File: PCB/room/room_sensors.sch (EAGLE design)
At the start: 37 parts, among them U1 BH1750FVI-TR, U2 BME280, U3 CCS811B-JOPD500, U4 SN65HVD11DR, U5 SN65HVD11DR, U6 SN65HVD11DR, U7 SN65HVD11DR, U8 MAX14830ETMT

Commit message: first version of schematic ready
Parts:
- removed U$12: NCP551SN18T1G, NCP551SN_snapEDA:NCP551SN18T1G
- removed U$14: NCP551SN25T1G, NCP551SN_snapEDA:NCP551SN25T1G
- added C13, C15, C16, C17, C27, C28, C29: 100nF 50V, rcl:C-EUC0805
- added C14: 1uF 16V, rcl:C-EUC0805
- added C18, C19, C20, C21, C22, C25, C30, C31: 4u7 16V, rcl:C-EUC0805
- added C23, C24: 1u 16V, rcl:C-EUC0805
- added C26: 220p, rcl:C-EUC0805
- added D1, D2, D3, D4: CDSOT23-0502B, CDSOT23-SM712_snapEDA:CDSOT23-SM712
- added R10, R11, R12, R13, R30, R8, R9: 4k7, rcl:R-EU_R1206
- added R14: 0R, rcl:R-EU_R1206
- added R15: 47k, rcl:R-EU_R1206
- added R16: 680R, rcl:R-EU_R1206
- added R17, R18, R20, R21, R23, R24, R26, R27, R29: 1k, rcl:R-EU_R1206
- added R19, R22, R25, R28: 120R, rcl:R-EU_R1206
- added R5: 33k, rcl:R-EU_R1206
- added R6, R7: 100k, rcl:R-EU_R1206
- added U$17, U$18: RT9043GB, NCP551SN_snapEDA:RT9043GB
- added Y1: X1G004171001800 12MHz, X1G0041710033_snapEDA:X1G0041710033
- C10, C9: value 100nF 50V -> 2u2 16V
- C2, C3, C4, C5, C6, C7, C8: device rcl:C-EUC1206 -> rcl:C-EUC0805
- R4: value 100R -> 4k7
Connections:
- removed net +1V8: C11.1, C8.1, U$12.OUT, U$3.DVDD
- removed net +2V5: C12.1, C7.1, U$14.OUT, U$3.AVDD
- new net +1V2: C11.1, C7.1, U$17.FB, U$17.OUT, U$3.DVDD
- new net +2V8: C12.1, C8.1, R6.2, U$18.OUT, U$3.AVDD
- new net AS312_OUT: U$7.REL, U8.*CTS0
- new net CLK_12M: U$3.XVCLK, U$4.MCLK, U8.XIN, Y1.OUT
- new net ESP32_EN1: R5.1, R7.2, U$18.FB
- new net MAX_IO0: U$8.1B, U8.GPIO0
- new net MAX_IO1: U$8.2B, U8.GPIO1
- new net MAX_IO10: U8.GPIO10
- new net MAX_IO11: U8.GPIO11
- new net MAX_IO12: U8.GPIO12
- new net MAX_IO13: U8.GPIO13
- new net MAX_IO14: U8.GPIO14
- new net MAX_IO15: U8.GPIO15
- new net MAX_IO2: U$8.3B, U8.GPIO2
- new net MAX_IO3: U$8.4B, U8.GPIO3
- new net MAX_IO4: U$8.5B, U8.GPIO4
- new net MAX_IO5: U$8.6B, U8.GPIO5
- new net MAX_IO6: U$8.7B, U8.GPIO6
- new net MAX_IO7: U$8.8B, U8.GPIO7
- new net MAX_IO8: U8.GPIO8
- new net MAX_IO9: U8.GPIO9
- new net N$10: U6.D, U8.TX3
- new net N$11: U6.R, U8.RX3
- new net N$12: U4.DE, U4.~RE, U8.*RTS0
- new net N$13: U5.DE, U5.~RE, U8.*RTS1
- new net N$14: C13.1, R12.2, U8.*RST
- new net N$15: U7.DE, U7.~RE, U8.*RTS2
- new net N$16: U6.DE, U6.~RE, U8.*RTS3
- new net N$17: C14.1, U8.V18
- new net N$18: C22.2, U$4.VMID
- new net N$19: U$4.SPKOUTP, U$5.1
- new net N$20: U$4.SPKOUTN, U$5.2
- new net N$21: C23.2, R14.2, U$6.-
- new net N$22: C24.2, C26.2, R15.2, R16.1, U$6.+
- new net N$23: C23.1, U$4.MICN
- new net N$24: C24.1, U$4.MICP
- new net N$25: C25.1, R16.2, U$4.MICBIAS
- new net N$26: C25.2, C26.1, R15.1
- new net N$27: C28.1, R17.1, U1.DVI
- new net N$28: U3.PWM, U3.SENSE
- new net N$29: R30.1, U3.!RESET
- new net N$3: U4.D, U8.TX0
- new net N$4: R5.2, R6.1
- new net N$5: U4.R, U8.RX0
- new net N$6: U5.D, U8.TX1
- new net N$7: U5.R, U8.RX1
- new net N$8: U7.D, U8.TX2
- new net N$9: U7.R, U8.RX2
- new net RS485_A1: D1.IO2, R18.2, R19.1, U4.A
- new net RS485_A2: D2.IO2, R21.2, R22.1, U5.A
- new net RS485_A3: D3.IO2, R24.2, R25.1, U7.A
- new net RS485_A4: D4.IO2, R27.2, R28.1, U6.A
- new net RS485_B1: D1.IO1, R19.2, R20.1, U4.B
- new net RS485_B2: D2.IO1, R22.2, R23.1, U5.B
- new net RS485_B3: D3.IO1, R25.2, R26.1, U7.B
- new net RS485_B4: D4.IO1, R28.2, R29.1, U6.B
- new net SPKGND: C18.2, C19.2, C20.2, C21.2, U$4.AGND, U$4.DGND, U$4.SPKGND
- new net SPKVDD: C18.1, C19.1, C20.1, C21.1, U$4.AVDD, U$4.DBVDD, U$4.DCVDD, U$4.SPKVDD
- net +3V3: now also C15.1, C16.1, C17.1, C27.1, C29.1, C30.1, C31.1, C5.1, R10.2, R11.2, R12.1, R13.1, R17.2, R18.1, R21.1, R24.1, R27.1, R30.2, R8.2, R9.2, U$17.IN, U$18.IN, U$7.VDD, U$8.1A, U$8.2A, U$8.3A, U$8.4A, U$8.5A, U$8.6A, U$8.7A, U$8.8A, U1.VCC, U2.CSB, U2.VDD, U2.VDDIO, U3.VDD, U4.VCC, U5.VCC, U6.VCC, U7.VCC, U8.LDOEN, U8.SPI/*I2C, U8.VA, U8.VEXT, U8.VL, Y1.VCC; no longer U$12.EN, U$12.IN, U$14.EN, U$14.IN
- net ESP32_BOOT: no longer C5.1
- net ESP32_EN: no longer C4.1
- net ESP32_IO0: now also R11.1, U$4.SCLK, U1.SCL
- net ESP32_IO1: now also U$4.DACDAT
- net ESP32_IO18: now also U8.SCLK/SCL
- net ESP32_IO19: now also U8.MISO/SDA
- net ESP32_IO2: now also R10.1, U$3.SIO_C
- net ESP32_IO21: now also R13.2, U8.*IRQ; no longer U$3.XVCLK
- net ESP32_IO23: now also U8.MOSI/A1; no longer U$3.HREF
- net ESP32_IO26: now also R9.1
- net ESP32_IO27: now also U$3.HREF; no longer U$3.SIO_C
- net ESP32_IO3: now also U$4.BCLK
- net ESP32_IO32: now also U$4.ADCDAT
- net ESP32_IO33: now also R8.1, U$4.SDIN, U1.SDA
- net ESP32_IO4: now also U$4.FRAME
- net ESP32_IO5: now also U8.*CS/A0
- net GND: now also C13.2, C14.2, C15.2, C16.2, C17.2, C22.1, C27.2, C28.2, C29.2, C30.2, C31.2, D1.GND, D2.GND, D3.GND, D4.GND, R14.1, R20.2, R23.2, R26.2, R29.2, R7.1, U$17.GND, U$18.GND, U$4.MODE, U$7.VSS, U1.ADDR, U1.GND, U2.GND, U2.SDO, U3.!WAKE, U3.ADDR, U3.EP, U4.GND, U5.GND, U6.GND, U7.GND, U8.AGND, U8.DGND, U8.EP, Y1.GND; no longer U$12.GND, U$14.GND
- net N$2: now also C4.1
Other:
- note added: "ADDRESS: 236"
- note added: "ADDRESS: 52"
- note added: "ADDRESS: 70"
- note added: "CAMERA"
- note added: "GAS SENSOR"
- note added: "HUMIDITY, PRESSURE, TEMPERATURE SENSOR"
- note added: "I2C pullups"
- note added: "LIGHT SENSOR"
- note added: "OSCILLATOR"
- note added: "PIR SENSOR"
- note added: "SPI TO UART"
- note removed: "MAX14830 SPI TO UART"
- note removed: "OV2640"
- note removed: "SENSORS"

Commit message: Placement done
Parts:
- added C32, C33, C34, C35: 100nF 50V, rcl:C-EUC0805
- renumbered U$1 to CON1, U$17 to U17, U$18 to U18, U$2 to CON2, U$3 to CON3, U$4 to U14, U$5 to SPR1, U$8 to S8
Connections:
- removed net ESP32_IO10: A1.SWP/SD3
- removed net ESP32_IO11: A1.SCS/CMD
- removed net ESP32_IO6: A1.SCK/CLK
- removed net ESP32_IO7: A1.SDO/SD0
- removed net ESP32_IO8: A1.SDI/SD1
- removed net ESP32_IO9: A1.SHD/SD2
- removed net RS485_A4: D4.IO2, R27.2, R28.1, U6.A
- removed net RS485_B4: D4.IO1, R28.2, R29.1, U6.B
- removed net SPKGND: C18.2, C19.2, C20.2, C21.2, U14.AGND, U14.DGND, U14.SPKGND
- removed net SPKVDD: C18.1, C19.1, C20.1, C21.1, U14.AVDD, U14.DBVDD, U14.DCVDD, U14.SPKVDD
- new net RS485_A0: CON2.1, D1.IO2, R18.2, R19.1, U4.A
- new net RS485_B0: CON2.2, D1.IO1, R19.2, R20.1, U4.B
- net +3V3: now also C18.1, C19.1, C20.1, C21.1, C32.1, C33.1, C34.1, C35.1, CON1.2, CON1.4, U14.AVDD, U14.DBVDD, U14.DCVDD, U14.SPKVDD, U17.EN, U18.EN
- net ESP32_IO0: now also CON1.13, U2.SCK, U3.SCL
- net ESP32_IO1: now also CON2.9
- net ESP32_IO12: now also CON2.11
- net ESP32_IO13: now also CON2.13
- net ESP32_IO14: now also CON2.12
- net ESP32_IO15: now also CON2.14
- net ESP32_IO25: now also A1.IO25
- net ESP32_IO3: now also CON2.10
- net ESP32_IO33: now also CON1.14, U2.SDI, U3.SDA
- net ESP32_IO35: no longer A1.IO25
- net GND: now also C18.2, C19.2, C20.2, C21.2, C32.2, C33.2, C34.2, C35.2, CON1.1, CON1.3, U14.AGND, U14.DGND, U14.SPKGND
- net MAX_IO10: now also CON1.10
- net MAX_IO11: now also CON1.12
- net MAX_IO12: now also CON1.11
- net MAX_IO13: now also CON1.9
- net MAX_IO14: now also CON1.7
- net MAX_IO15: now also CON1.5
- net MAX_IO8: now also CON1.6
- net MAX_IO9: now also CON1.8
- net RS485_A1: now also CON2.3, D2.IO2, R21.2, R22.1, U5.A; no longer D1.IO2, R18.2, R19.1, U4.A
- net RS485_A2: now also CON2.5, D3.IO2, R24.2, R25.1, U7.A; no longer D2.IO2, R21.2, R22.1, U5.A
- net RS485_A3: now also CON2.7, D4.IO2, R27.2, R28.1, U6.A; no longer D3.IO2, R24.2, R25.1, U7.A
- net RS485_B1: now also CON2.4, D2.IO1, R22.2, R23.1, U5.B; no longer D1.IO1, R19.2, R20.1, U4.B
- net RS485_B2: now also CON2.6, D3.IO1, R25.2, R26.1, U7.B; no longer D2.IO1, R22.2, R23.1, U5.B
- net RS485_B3: now also CON2.8, D4.IO1, R28.2, R29.1, U6.B; no longer D3.IO1, R25.2, R26.1, U7.B
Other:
- note added: "CONNECTORS"
- note removed: "CONNECTOR"
- moved on the sheet: C15, C16, C17, C3, R1

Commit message: finished routing for room sensor PCB
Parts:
- removed C16: 100nF 50V, rcl:C-EUC0805
- added C36: 100nF 50V, rcl:C-EUC0805
- added C37: NM, rcl:C-EUC0805
- added C38: 1uF 16V, rcl:C-EUC0805
- added C39, C40: 47u 10V, rcl:C-EUC1210
- added C41, C42: 100n 50V, rcl:C-EUC1206
- added C43, C44: 2u2 50V, rcl:C-EUC1206
- added C45, C46: 47u 35V, rcl:CPOL-EUUD-5X5,8
- added D5, D6: B360B-13-F, diode:MBRS130LT3
- added L2: 5u6 3A8, parts:SLF10145T-150M2R2-PF
- added LOGO1: OSHW_LOGO_FILLX0350-NT, ohw-logo:OSHW_LOGO_FILLX0350-NT
- added R31: 0R, rcl:R-EU_R0603
- added R32: 1k, rcl:R-EU_R1206
- added R33: 33k, rcl:R-EU_R1206
- added R34: 12k, rcl:R-EU_R1206
- added R35: 68k, rcl:R-EU_R1206
- added R36: 100k, rcl:R-EU_R1206
- added U12: LMR16020, LMR160X0_snapEDA:LMR16020
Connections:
- new net +24V: C42.1, C43.1, C44.1, C45.+, C46.+, D6.C, U12.EN, U12.VIN
- new net N$30: C21.2, R31.2, U14.SPKVDD
- new net N$31: CON1.2, D6.A
- new net N$32: R33.1, U12.RT/SYNC
- new net N$33: C37.2, R34.1, R35.2, R36.2, U12.FB
- new net N$34: C41.2, D5.C, L2.1, U12.SW
- new net N$35: C41.1, U12.BOOT
- net +3V3: now also C36.1, C37.1, C38.1, C39.1, C40.1, L2.2, R31.1, R32.2, R35.1, R36.1; no longer C16.1, C21.1, CON1.2, U14.SPKVDD
- net AS312_OUT: now also R32.1
- net GND: now also C21.1, C36.2, C38.2, C39.2, C40.2, C42.2, C43.2, C44.2, C45.-, C46.-, D5.A, R33.2, R34.2, U12.GND; no longer C16.2, C21.2
- net N$10: now also U4.D; no longer U6.D
- net N$11: now also U4.R; no longer U6.R
- net N$12: now also U7.DE, U7.~RE; no longer U4.DE, U4.~RE
- net N$13: now also U6.DE, U6.~RE; no longer U5.DE, U5.~RE
- net N$15: now also U5.DE, U5.~RE; no longer U7.DE, U7.~RE
- net N$16: now also U4.DE, U4.~RE; no longer U6.DE, U6.~RE
- net N$3: now also U7.D; no longer U4.D
- net N$5: now also U7.R; no longer U4.R
- net N$6: now also U6.D; no longer U5.D
- net N$7: now also U6.R; no longer U5.R
- net N$8: now also U5.D; no longer U7.D
- net N$9: now also U5.R; no longer U7.R
- net RS485_A0: now also U7.A; no longer U4.A
- net RS485_A1: now also U6.A; no longer U5.A
- net RS485_A2: now also U5.A; no longer U7.A
- net RS485_A3: now also U4.A; no longer U6.A
- net RS485_B0: now also U7.B; no longer U4.B
- net RS485_B1: now also U6.B; no longer U5.B
- net RS485_B2: now also U5.B; no longer U7.B
- net RS485_B3: now also U4.B; no longer U6.B

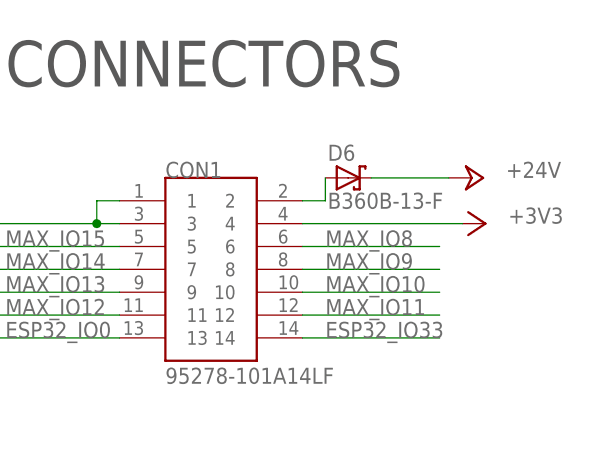
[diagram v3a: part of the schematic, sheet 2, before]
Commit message: finished interface PCB
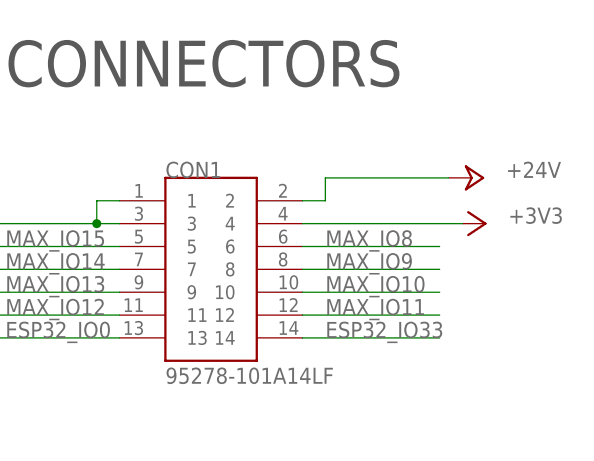
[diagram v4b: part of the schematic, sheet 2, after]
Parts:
- removed D6: B360B-13-F, diode:MBRS130LT3
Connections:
- removed net N$31: CON1.2, D6.A
- net +24V: now also CON1.2; no longer D6.C
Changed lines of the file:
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@@
 <part name="U6" library="SN65HVD11DR_snapEDA" deviceset="SN65HVD11DR" device=""/>
 <part name="U7" library="SN65HVD11DR_snapEDA" deviceset="SN65HVD11DR" device=""/>
-<part name="D6" library="diode" deviceset="MBRS130LT3" device="" value="B360B-13-F"/>
 </parts>
 <sheets>
@@
 <attribute name="VALUE" x="236.22" y="132.08" size="1.778" layer="96"/>
 </instance>
-<instance part="D6" gate="G$1" x="218.44" y="137.16"/>
 </instances>
 <busses>
@@
 </segment>
 </net>
-<net name="N$31" class="0">
-<segment>
+<net name="+24V" class="0">
+<segment>
+<wire x1="215.9" y1="137.16" x2="229.616" y2="137.16" width="0.1524" layer="91"/>
+<pinref part="P+1" gate="1" pin="+24V"/>
 <pinref part="CON1" gate="G$1" pin="2"/>
-<pinref part="D6" gate="G$1" pin="A"/>
 <wire x1="213.36" y1="134.62" x2="215.9" y2="134.62" width="0.1524" layer="91"/>
 <wire x1="215.9" y1="134.62" x2="215.9" y2="137.16" width="0.1524" layer="91"/>
 </segment>
 </net>
-<net name="+24V" class="0">
-<segment>
-<pinref part="D6" gate="G$1" pin="C"/>
-<wire x1="220.98" y1="137.16" x2="229.616" y2="137.16" width="0.1524" layer="91"/>
-<pinref part="P+1" gate="1" pin="+24V"/>
-</segment>
-</net>
